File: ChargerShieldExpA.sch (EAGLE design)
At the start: 85 parts, among them IC1 LM324N, IC2 TL431, Q1 BD648, Q2 BUZ11, Q3 BUZ171, T2 BC548, X1 +5V, X2 Battery, X3 VCC

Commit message: arrangement
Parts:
- added JP15: (no value), bigger:JP1E
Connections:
- new net N$35: JP15.2, R17.1
- net N$17: now also JP15.1; no longer R17.1
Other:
- moved on the sheet: R17
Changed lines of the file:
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@@
 <grid distance="0.05" unitdist="inch" unit="mm" style="lines" multiple="1" display="yes" altdistance="0.025" altunitdist="inch" altunit="mm"/>
 <layers>
-<layer number="1" name="Top" color="4" fill="1" visible="yes" active="no"/>
-<layer number="2" name="Route2" color="1" fill="3" visible="yes" active="no"/>
-<layer number="3" name="Route3" color="4" fill="3" visible="yes" active="no"/>
-<layer number="4" name="Route4" color="1" fill="4" visible="yes" active="no"/>
-<layer number="5" name="Route5" color="4" fill="4" visible="yes" active="no"/>
-<layer number="6" name="Route6" color="1" fill="8" visible="yes" active="no"/>
-<layer number="7" name="Route7" color="4" fill="8" visible="yes" active="no"/>
-<layer number="8" name="Route8" color="1" fill="2" visible="yes" active="no"/>
-<layer number="9" name="Route9" color="4" fill="2" visible="yes" active="no"/>
-<layer number="10" name="Route10" color="1" fill="7" visible="yes" active="no"/>
-<layer number="11" name="Route11" color="4" fill="7" visible="yes" active="no"/>
-<layer number="12" name="Route12" color="1" fill="5" visible="yes" active="no"/>
-<layer number="13" name="Route13" color="4" fill="5" visible="yes" active="no"/>
-<layer number="14" name="Route14" color="1" fill="6" visible="yes" active="no"/>
-<layer number="15" name="Route15" color="4" fill="6" visible="yes" active="no"/>
-<layer number="16" name="Bottom" color="1" fill="1" visible="yes" active="no"/>
-<layer number="17" name="Pads" color="2" fill="1" visible="yes" active="no"/>
-<layer number="18" name="Vias" color="2" fill="1" visible="yes" active="no"/>
-<layer number="19" name="Unrouted" color="6" fill="1" visible="yes" active="no"/>
-<layer number="20" name="Dimension" color="15" fill="1" visible="yes" active="no"/>
-<layer number="21" name="tPlace" color="7" fill="1" visible="yes" active="no"/>
-<layer number="22" name="bPlace" color="7" fill="1" visible="yes" active="no"/>
-<layer number="23" name="tOrigins" color="15" fill="1" visible="yes" active="no"/>
-<layer number="24" name="bOrigins" color="15" fill="1" visible="yes" active="no"/>
-<layer number="25" name="tNames" color="7" fill="1" visible="yes" active="no"/>
-<layer number="26" name="bNames" color="7" fill="1" visible="yes" active="no"/>
-<layer number="27" name="tValues" color="7" fill="1" visible="yes" active="no"/>
-<layer number="28" name="bValues" color="7" fill="1" visible="yes" active="no"/>
+<layer number="1" name="Top" color="4" fill="1" visible="no" active="no"/>
+<layer number="2" name="Route2" color="1" fill="3" visible="no" active="no"/>
+<layer number="3" name="Route3" color="4" fill="3" visible="no" active="no"/>
+<layer number="4" name="Route4" color="1" fill="4" visible="no" active="no"/>
+<layer number="5" name="Route5" color="4" fill="4" visible="no" active="no"/>
+<layer number="6" name="Route6" color="1" fill="8" visible="no" active="no"/>
+<layer number="7" name="Route7" color="4" fill="8" visible="no" active="no"/>
+<layer number="8" name="Route8" color="1" fill="2" visible="no" active="no"/>
+<layer number="9" name="Route9" color="4" fill="2" visible="no" active="no"/>
+<layer number="10" name="Route10" color="1" fill="7" visible="no" active="no"/>
+<layer number="11" name="Route11" color="4" fill="7" visible="no" active="no"/>
+<layer number="12" name="Route12" color="1" fill="5" visible="no" active="no"/>
+<layer number="13" name="Route13" color="4" fill="5" visible="no" active="no"/>
+<layer number="14" name="Route14" color="1" fill="6" visible="no" active="no"/>
+<layer number="15" name="Route15" color="4" fill="6" visible="no" active="no"/>
+<layer number="16" name="Bottom" color="1" fill="1" visible="no" active="no"/>
+<layer number="17" name="Pads" color="2" fill="1" visible="no" active="no"/>
+<layer number="18" name="Vias" color="2" fill="1" visible="no" active="no"/>
+<layer number="19" name="Unrouted" color="6" fill="1" visible="no" active="no"/>
+<layer number="20" name="Dimension" color="15" fill="1" visible="no" active="no"/>
+<layer number="21" name="tPlace" color="7" fill="1" visible="no" active="no"/>
+<layer number="22" name="bPlace" color="7" fill="1" visible="no" active="no"/>
+<layer number="23" name="tOrigins" color="15" fill="1" visible="no" active="no"/>
+<layer number="24" name="bOrigins" color="15" fill="1" visible="no" active="no"/>
+<layer number="25" name="tNames" color="7" fill="1" visible="no" active="no"/>
+<layer number="26" name="bNames" color="7" fill="1" visible="no" active="no"/>
+<layer number="27" name="tValues" color="7" fill="1" visible="no" active="no"/>
+<layer number="28" name="bValues" color="7" fill="1" visible="no" active="no"/>
 <layer number="29" name="tStop" color="7" fill="3" visible="no" active="no"/>
 <layer number="30" name="bStop" color="7" fill="6" visible="no" active="no"/>
@@
 <layer number="35" name="tGlue" color="7" fill="4" visible="no" active="no"/>
 <layer number="36" name="bGlue" color="7" fill="5" visible="no" active="no"/>
-<layer number="37" name="tTest" color="7" fill="1" visible="yes" active="no"/>
-<layer number="38" name="bTest" color="7" fill="1" visible="yes" active="no"/>
+<layer number="37" name="tTest" color="7" fill="1" visible="no" active="no"/>
+<layer number="38" name="bTest" color="7" fill="1" visible="no" active="no"/>
 <layer number="39" name="tKeepout" color="4" fill="11" visible="no" active="no"/>
 <layer number="40" name="bKeepout" color="1" fill="11" visible="no" active="no"/>
@@
 <layer number="44" name="Drills" color="7" fill="1" visible="no" active="no"/>
 <layer number="45" name="Holes" color="7" fill="1" visible="no" active="no"/>
-<layer number="46" name="Milling" color="3" fill="1" visible="yes" active="no"/>
-<layer number="47" name="Measures" color="7" fill="1" visible="yes" active="no"/>
-<layer number="48" name="Document" color="7" fill="1" visible="yes" active="no"/>
-<layer number="49" name="Reference" color="7" fill="1" visible="yes" active="no"/>
-<layer number="50" name="dxf" color="7" fill="1" visible="yes" active="no"/>
-<layer number="51" name="tDocu" color="7" fill="1" visible="yes" active="no"/>
-<layer number="52" name="bDocu" color="7" fill="1" visible="yes" active="no"/>
-<layer number="53" name="tGND_GNDA" color="7" fill="9" visible="yes" active="no"/>
-<layer number="54" name="bGND_GNDA" color="1" fill="9" visible="yes" active="no"/>
-<layer number="56" name="wert" color="7" fill="1" visible="yes" active="no"/>
-<layer number="57" name="tCAD" color="7" fill="1" visible="yes" active="no"/>
+<layer number="46" name="Milling" color="3" fill="1" visible="no" active="no"/>
+<layer number="47" name="Measures" color="7" fill="1" visible="no" active="no"/>
+<layer number="48" name="Document" color="7" fill="1" visible="no" active="no"/>
+<layer number="49" name="Reference" color="7" fill="1" visible="no" active="no"/>
+<layer number="50" name="dxf" color="7" fill="1" visible="no" active="no"/>
+<layer number="51" name="tDocu" color="7" fill="1" visible="no" active="no"/>
+<layer number="52" name="bDocu" color="7" fill="1" visible="no" active="no"/>
+<layer number="53" name="tGND_GNDA" color="7" fill="9" visible="no" active="no"/>
+<layer number="54" name="bGND_GNDA" color="1" fill="9" visible="no" active="no"/>
+<layer number="56" name="wert" color="7" fill="1" visible="no" active="no"/>
+<layer number="57" name="tCAD" color="7" fill="1" visible="no" active="no"/>
 <layer number="91" name="Nets" color="2" fill="1" visible="yes" active="yes"/>
 <layer number="92" name="Busses" color="1" fill="1" visible="yes" active="yes"/>
@@
 <part name="R35" library="rcl" deviceset="R-EU_" device="0204/7" value="100k"/>
 <part name="GND9" library="supply1" deviceset="GND" device=""/>
+<part name="JP15" library="bigger" deviceset="JP1E" device=""/>
 </parts>
 <sheets>
@@
 <instance part="R16" gate="G$1" x="102.87" y="30.48" rot="R90"/>
 <instance part="GND11" gate="1" x="99.06" y="19.05"/>
-<instance part="R17" gate="G$1" x="107.95" y="54.61"/>
+<instance part="R17" gate="G$1" x="115.57" y="54.61"/>
 <instance part="R18" gate="G$1" x="95.25" y="30.48" rot="R90"/>
 <instance part="IC1" gate="P" x="26.67" y="38.1"/>
@@
 <instance part="R35" gate="G$1" x="181.61" y="76.2" rot="R90"/>
 <instance part="GND9" gate="1" x="181.61" y="60.96"/>
+<instance part="JP15" gate="A" x="105.41" y="57.15"/>
 </instances>
 <busses>
@@
 <pinref part="R15" gate="G$1" pin="2"/>
 <wire x1="99.06" y1="54.61" x2="99.06" y2="48.26" width="0.1524" layer="91"/>
-<wire x1="99.06" y1="54.61" x2="102.87" y2="54.61" width="0.1524" layer="91"/>
+<wire x1="99.06" y1="54.61" x2="105.41" y2="54.61" width="0.1524" layer="91"/>
 <junction x="99.06" y="54.61"/>
-<pinref part="R17" gate="G$1" pin="1"/>
+<pinref part="JP15" gate="A" pin="1"/>
 </segment>
 </net>
 <net name="I_DISC1" class="0">
 <segment>
+<label x="127" y="54.61" size="1.778" layer="95" xref="yes"/>
+<wire x1="120.65" y1="54.61" x2="127" y2="54.61" width="0.1524" layer="91"/>
 <pinref part="R17" gate="G$1" pin="2"/>
-<wire x1="113.03" y1="54.61" x2="116.84" y2="54.61" width="0.1524" layer="91"/>
-<label x="116.84" y="54.61" size="1.778" layer="95" xref="yes"/>
 </segment>
 </net>
@@
 </segment>
 </net>
+<net name="N$35" class="0">
+<segment>
+<pinref part="R17" gate="G$1" pin="1"/>
+<pinref part="JP15" gate="A" pin="2"/>
+<wire x1="107.95" y1="54.61" x2="110.49" y2="54.61" width="0.1524" layer="91"/>
+</segment>
+</net>

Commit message: power pins, Vin
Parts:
- added JP16, JP17, JP18: (no value), bigger:JP2E
- R4: device rcl:R-EU_0207/10 -> rcl:R-EU_0207/15
- X1: value +5V -> +Vin
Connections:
- new net N$50: JP17.1, JP17.2, JP17.3, U$1.VIN, X1-1.KL
- net +5V: now also JP16.1, JP16.2, JP16.3; no longer X1-1.KL
- net GND: now also JP18.1, JP18.2, JP18.3

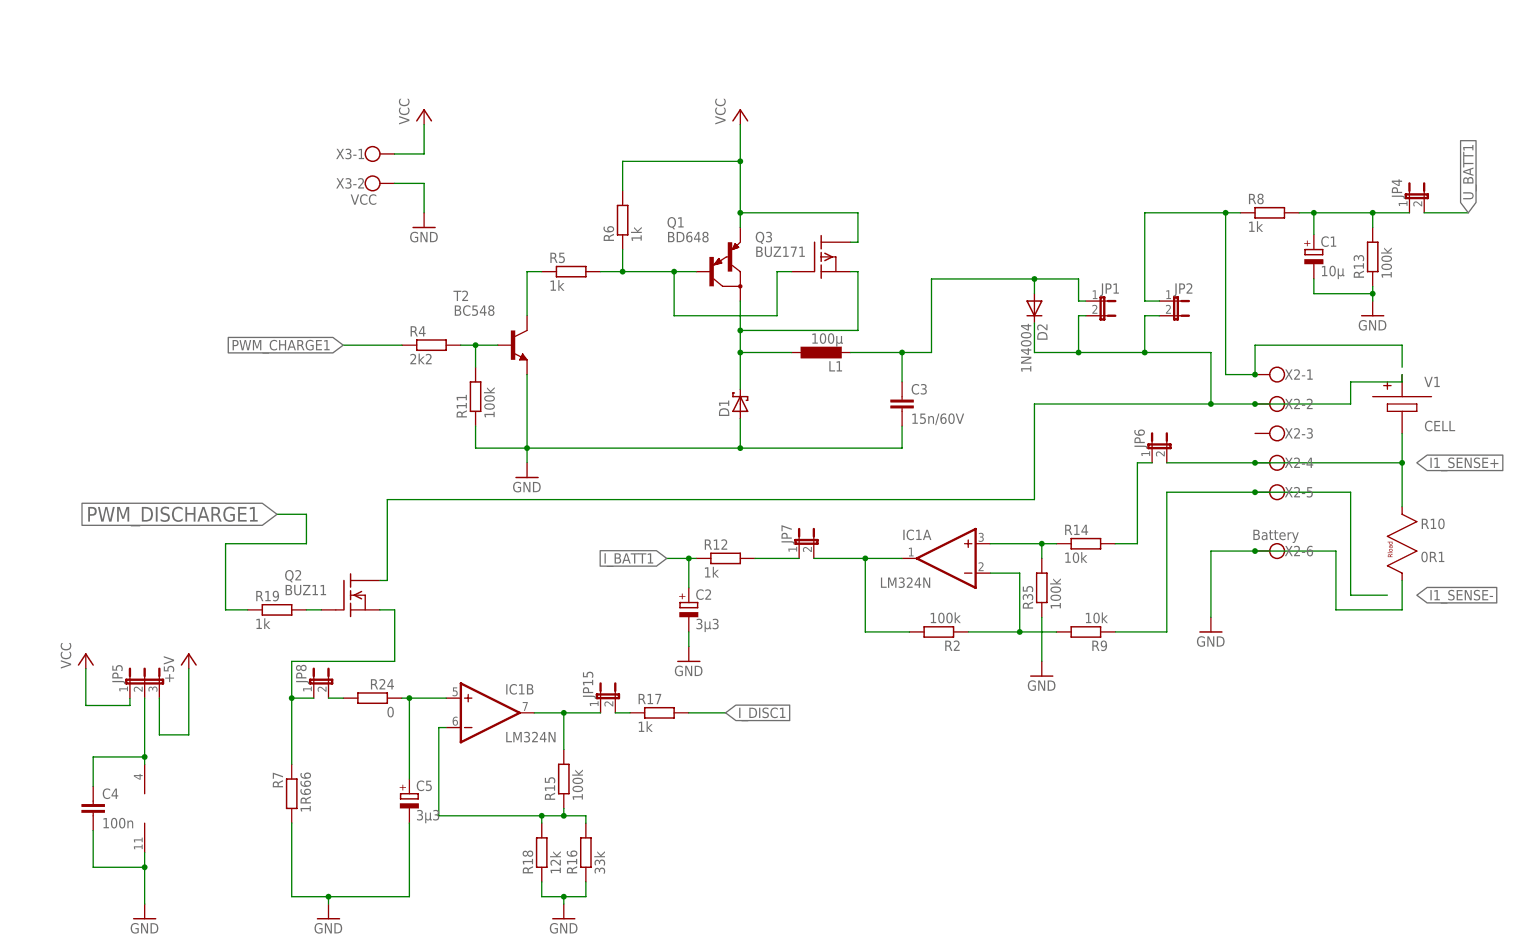
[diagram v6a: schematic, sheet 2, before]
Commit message: boost converter
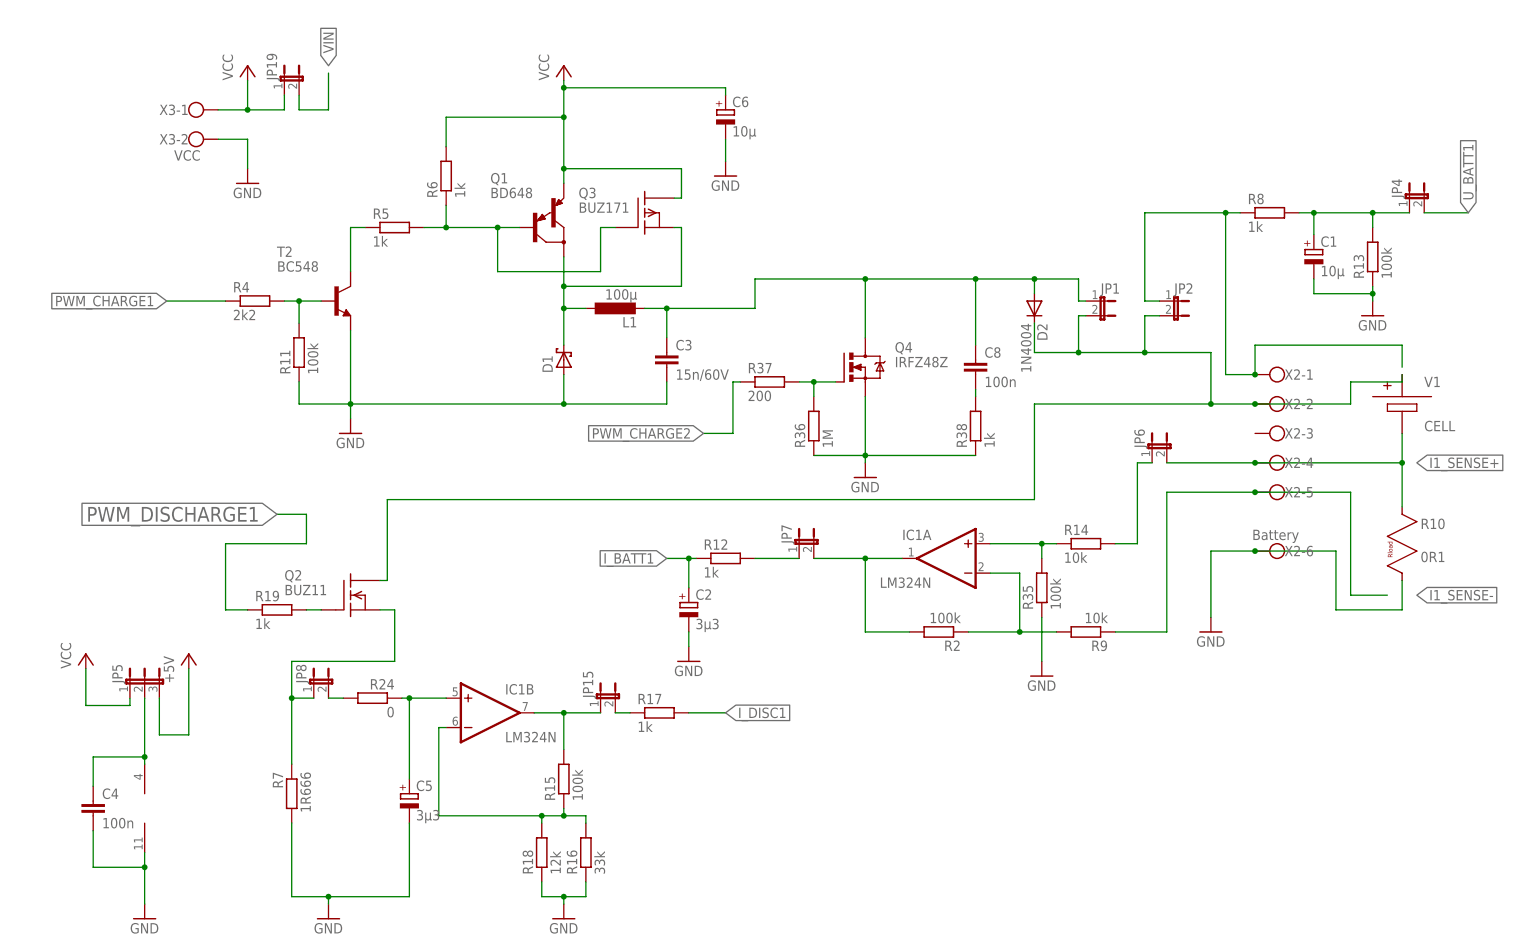
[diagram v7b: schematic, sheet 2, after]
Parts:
- added C6: 10µ, rcl:CPOL-EUE5-5
- added C8: 100n, rcl:C-EU025_050-025X075
- added JP19: (no value), bigger:JP1E
- added Q4: IRFZ48Z, transistor-power:IRFZ48Z
- added R36: 1M, rcl:R-EU_0207/10
- added R37: 200, rcl:R-EU_0207/12
- added R38: 1k, rcl:R-EU_0207/10
- R19: device rcl:R-EU_0207/12 -> rcl:R-EU_0204/7
- R9: device rcl:R-EU_0207/12 -> rcl:R-EU_0207/10
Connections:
- new net N$51: Q4.G, R36.2, R37.2
- new net VIN: JP17.1, JP17.2, JP17.3, JP19.2, U$1.VIN, X1-1.KL
- net GND: now also C6.-, Q4.S, R36.1, R38.1
- net N$10: now also C8.1, Q4.D
- net N$50: now also C8.2, R38.2; no longer JP17.1, JP17.2, JP17.3, U$1.VIN, X1-1.KL
- net PWM_CHARGE2: now also R37.1
- net VCC: now also C6.+, JP19.1
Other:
- moved on the sheet: C3, D1, L1, Q1, Q3, R11, R4, R5, R6, T2, X3-1, X3-2

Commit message: tidy up
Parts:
- added JP20: (no value), bigger:JP2E
- added JP21, JP22: (no value), bigger:JP1E
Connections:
- removed net GND2: LED1.C, LED2.C, LED3.C, LED4.C, LED5.C, LED6.C, S1.1, S2.1, S3.1, S4.1, S5.1, S6.1, U$3.1, U$6.1
- new net N$52: JP21.1, U$1.D0
- new net N$53: JP22.1, U$1./RESET
- net +5V: now also JP3.3, U$2.VCC
- net GND: now also JP22.2, LED1.C, LED2.C, LED3.C, LED4.C, LED5.C, LED6.C, S1.1, S2.1, S3.1, S4.1, S5.1, S6.1, U$3.1, U$6.1; no longer JP3.3, U$2.VCC
- net I_BATT2: now also JP20.2
- net I_DISC2: now also JP20.3
- net N$37: now also U$1.D6
- net N$38: now also U$1.SDA
- net N$41: now also R27.1, U$1.SCL, U$5.7, U$6.7; no longer R26.1, U$5.6, U$6.6
- net N$42: now also JP21.2, R26.1, U$1.D1, U$5.6, U$6.6; no longer R27.1, U$5.7, U$6.7
- net U_BATT2: now also JP20.1
